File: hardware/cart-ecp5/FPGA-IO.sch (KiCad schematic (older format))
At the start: 9 parts, among them U1 LFE5U-25F-xBG256x, U5 W25Q128JVSIM

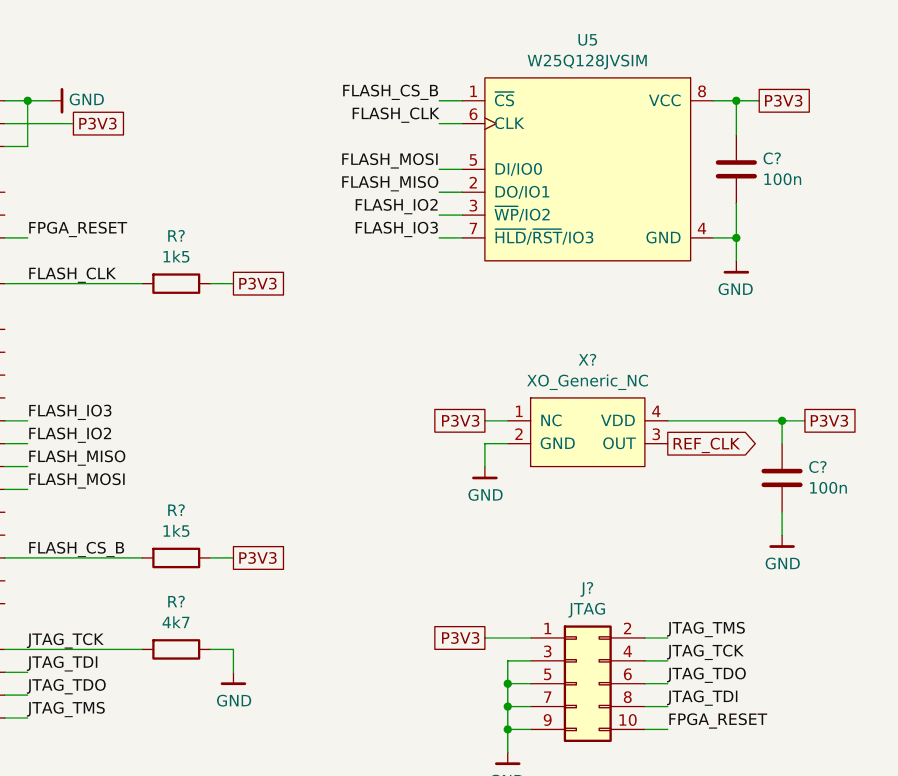
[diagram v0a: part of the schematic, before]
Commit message: First pass annotation and footprint assignment complete
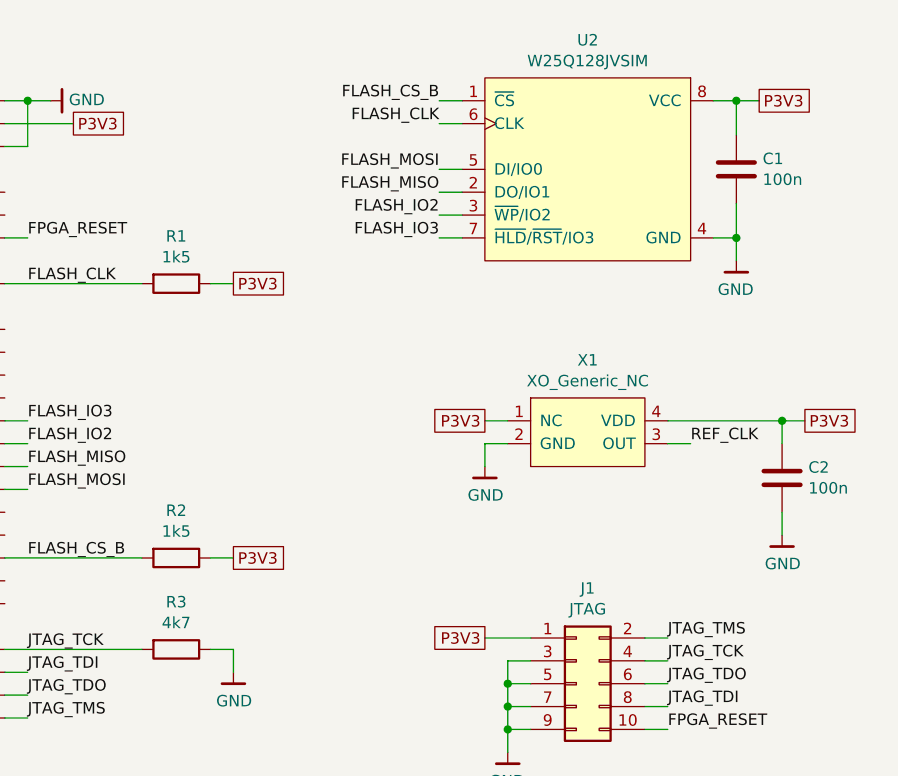
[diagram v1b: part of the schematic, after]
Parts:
- J1: renamed from J?; footprint Connector_PinHeader_1.27mm:PinHeader_2x05_P1.27mm_Vertical_SMD -> Connector_PinHeader_2.54mm:PinHeader_2x05_P2.54mm_Vertical
- R1, R2, R3: renamed from R?; footprint (none) -> Resistor_SMD:R_0603_1608Metric
- gave numbers to parts that had none: 3
- renumbered U5 to U2
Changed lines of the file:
@@
 $EndDescr
 $Comp
-L ng_memory:W25Q128JVSIM U5
+L ng_memory:W25Q128JVSIM U2
 U 1 1 5F3FC315
 P 13200 1500
-F 0 "U5" H 13650 1665 50  0000 C CNN
+F 0 "U2" H 13650 1665 50  0000 C CNN
 F 1 "W25Q128JVSIM" H 13650 1574 50  0000 C CNN
 F 2 "Package_SO:SOIC-8_5.275x5.275mm_P1.27mm" H 13700 650 50  0001 C CNN
@@
 	10200 4300 10300 4300
 $Comp
-L ng_power:GND #PWR?
+L ng_power:GND #PWR03
 U 1 1 5F643215
 P 10400 1600
-F 0 "#PWR?" H 10400 1350 50  0001 C CNN
+F 0 "#PWR03" H 10400 1350 50  0001 C CNN
 F 1 "GND" V 10404 1520 50  0000 R CNN
 F 2 "" H 10300 1250 50  0001 C CNN
@@
 	10200 2200 10300 2200
 $Comp
-L Device:R R?
+L Device:R R3
 U 1 1 5F64C834
 P 10950 4000
-F 0 "R?" V 10743 4000 50  0000 C CNN
+F 0 "R3" V 10743 4000 50  0000 C CNN
 F 1 "4k7" V 10834 4000 50  0000 C CNN
-F 2 "" V 10880 4000 50  0001 C CNN
+F 2 "Resistor_SMD:R_0603_1608Metric" V 10880 4000 50  0001 C CNN
 F 3 "~" H 10950 4000 50  0001 C CNN
 	1    10950 4000
@@
 $EndComp
 $Comp
-L Connector_Generic:Conn_02x05_Odd_Even J?
+L Connector_Generic:Conn_02x05_Odd_Even J1
 U 1 1 5F651B0D
 P 12700 4150
-F 0 "J?" H 12750 4567 50  0000 C CNN
+F 0 "J1" H 12750 4567 50  0000 C CNN
 F 1 "JTAG" H 12750 4476 50  0000 C CNN
-F 2 "Connector_PinHeader_1.27mm:PinHeader_2x05_P1.27mm_Vertical_SMD" H 12700 4150 50  0001 C CNN
+F 2 "Connector_PinHeader_2.54mm:PinHeader_2x05_P2.54mm_Vertical" H 12700 4150 50  0001 C CNN
 F 3 "~" H 12700 4150 50  0001 C CNN
 	1    12700 4150
@@
 	11200 4000 11200 4100
 $Comp
-L ng_power:GND #PWR?
+L ng_power:GND #PWR04
 U 1 1 5F666BF6
 P 11200 4100
-F 0 "#PWR?" H 11200 3850 50  0001 C CNN
+F 0 "#PWR04" H 11200 3850 50  0001 C CNN
 F 1 "GND" H 11203 3974 50  0000 C CNN
 F 2 "" H 11100 3750 50  0001 C CNN
@@
 FPGA_RESET
 $Comp
-L ng_power:GND #PWR?
+L ng_power:GND #PWR06
 U 1 1 5F676420
 P 12400 4450
-F 0 "#PWR?" H 12400 4200 50  0001 C CNN
+F 0 "#PWR06" H 12400 4200 50  0001 C CNN
 F 1 "GND" H 12403 4324 50  0000 C CNN
 F 2 "" H 12300 4100 50  0001 C CNN
@@
 $EndComp
 $Comp
-L Device:R R?
+L Device:R R1
 U 1 1 5F67946D
 P 10950 2400
-F 0 "R?" V 10743 2400 50  0000 C CNN
+F 0 "R1" V 10743 2400 50  0000 C CNN
 F 1 "1k5" V 10834 2400 50  0000 C CNN
-F 2 "" V 10880 2400 50  0001 C CNN
+F 2 "Resistor_SMD:R_0603_1608Metric" V 10880 2400 50  0001 C CNN
 F 3 "~" H 10950 2400 50  0001 C CNN
 	1    10950 2400
@@
 	11100 2400 11200 2400
 $Comp
-L Device:R R?
+L Device:R R2
 U 1 1 5F67D9E4
 P 10950 3600
-F 0 "R?" V 10743 3600 50  0000 C CNN
+F 0 "R2" V 10743 3600 50  0000 C CNN
 F 1 "1k5" V 10834 3600 50  0000 C CNN
-F 2 "" V 10880 3600 50  0001 C CNN
+F 2 "Resistor_SMD:R_0603_1608Metric" V 10880 3600 50  0001 C CNN
 F 3 "~" H 10950 3600 50  0001 C CNN
 	1    10950 3600
@@
 $EndComp
 $Comp
-L ng_time:XO_Generic_NC X?
+L ng_time:XO_Generic_NC X1
 U 1 1 5F7FED75
 P 12750 3050
-F 0 "X?" H 12750 3365 50  0000 C CNN
+F 0 "X1" H 12750 3365 50  0000 C CNN
 F 1 "XO_Generic_NC" H 12750 3274 50  0000 C CNN
 F 2 "ng_time:Oscillator_2.5x2.0" H 12750 2950 50  0001 C CNN
@@
 P3V3
 $Comp
-L ng_power:GND #PWR?
+L ng_power:GND #PWR05
 U 1 1 5F809997
 P 12300 3200
-F 0 "#PWR?" H 12300 2950 50  0001 C CNN
+F 0 "#PWR05" H 12300 2950 50  0001 C CNN
 F 1 "GND" H 12303 3074 50  0000 C CNN
 F 2 "" H 12200 2850 50  0001 C CNN
@@
 	1    0    0    -1
 $EndComp
-Text GLabel 13100 3100 2    50   Output ~ 0
-REF_CLK
-$Comp
-L Device:C C?
+$Comp
+L Device:C C1
 U 1 1 5F81782E
 P 13400 1900
-F 0 "C?" H 13515 1946 50  0000 L CNN
+F 0 "C1" H 13515 1946 50  0000 L CNN
 F 1 "100n" H 13515 1855 50  0000 L CNN
 F 2 "" H 13438 1750 50  0001 C CNN
@@
 Connection ~ 13400 2200
 $Comp
-L ng_power:GND #PWR?
+L ng_power:GND #PWR07
 U 1 1 5F8236E3
 P 13400 2300
-F 0 "#PWR?" H 13400 2050 50  0001 C CNN
+F 0 "#PWR07" H 13400 2050 50  0001 C CNN
 F 1 "GND" H 13403 2174 50  0000 C CNN
 F 2 "" H 13300 1950 50  0001 C CNN
@@
 P3V3
 $Comp
-L Device:C C?
+L Device:C C2
 U 1 1 5F839810
 P 13600 3250
-F 0 "C?" H 13715 3296 50  0000 L CNN
+F 0 "C2" H 13715 3296 50  0000 L CNN
 F 1 "100n" H 13715 3205 50  0000 L CNN
 F 2 "" H 13638 3100 50  0001 C CNN
@@
 	13600 3000 13700 3000
 $Comp
-L ng_power:GND #PWR?
+L ng_power:GND #PWR08
 U 1 1 5F83DBF8
 P 13600 3500
-F 0 "#PWR?" H 13600 3250 50  0001 C CNN
+F 0 "#PWR08" H 13600 3250 50  0001 C CNN
 F 1 "GND" H 13603 3374 50  0000 C CNN
 F 2 "" H 13500 3150 50  0001 C CNN
@@
 	13600 3000 13100 3000
 Connection ~ 13600 3000
+Wire Wire Line
+	13100 3100 13200 3100
+Text Label 13200 3100 0    50   ~ 0
+REF_CLK
 $EndSCHEMATC

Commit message: Fixes for footprint assignment
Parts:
- C1, C2: footprint (none) -> Capacitor_SMD:C_0603_1608Metric
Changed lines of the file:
@@
 F 0 "C1" H 13515 1946 50  0000 L CNN
 F 1 "100n" H 13515 1855 50  0000 L CNN
-F 2 "" H 13438 1750 50  0001 C CNN
+F 2 "Capacitor_SMD:C_0603_1608Metric" H 13438 1750 50  0001 C CNN
 F 3 "~" H 13400 1900 50  0001 C CNN
 	1    13400 1900
@@
 F 0 "C2" H 13715 3296 50  0000 L CNN
 F 1 "100n" H 13715 3205 50  0000 L CNN
-F 2 "" H 13638 3100 50  0001 C CNN
+F 2 "Capacitor_SMD:C_0603_1608Metric" H 13638 3100 50  0001 C CNN
 F 3 "~" H 13600 3250 50  0001 C CNN
 	1    13600 3250

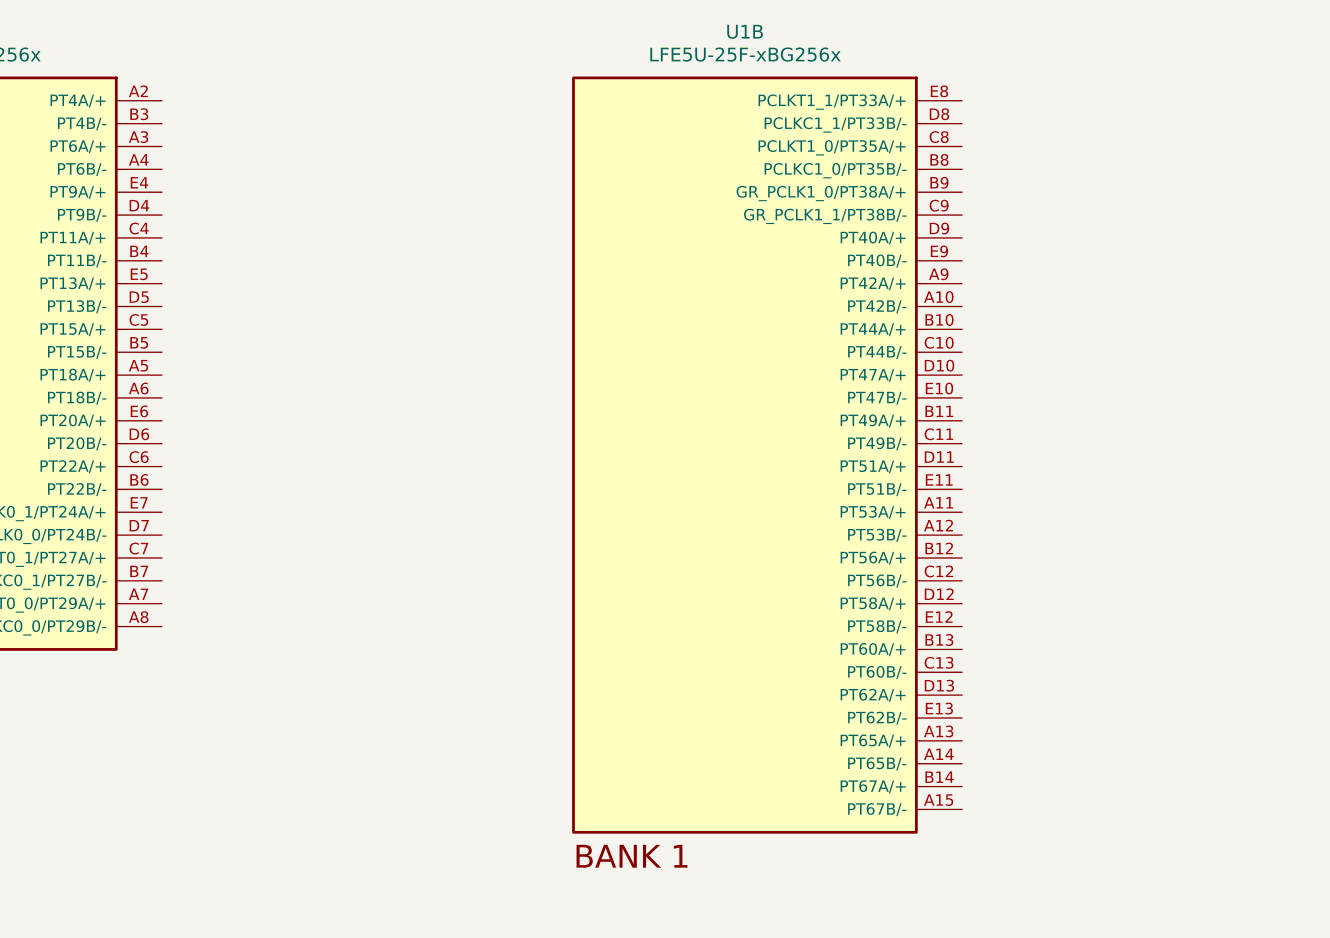
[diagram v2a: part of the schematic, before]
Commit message: Assign FPGA pins for N64 cartridge bus
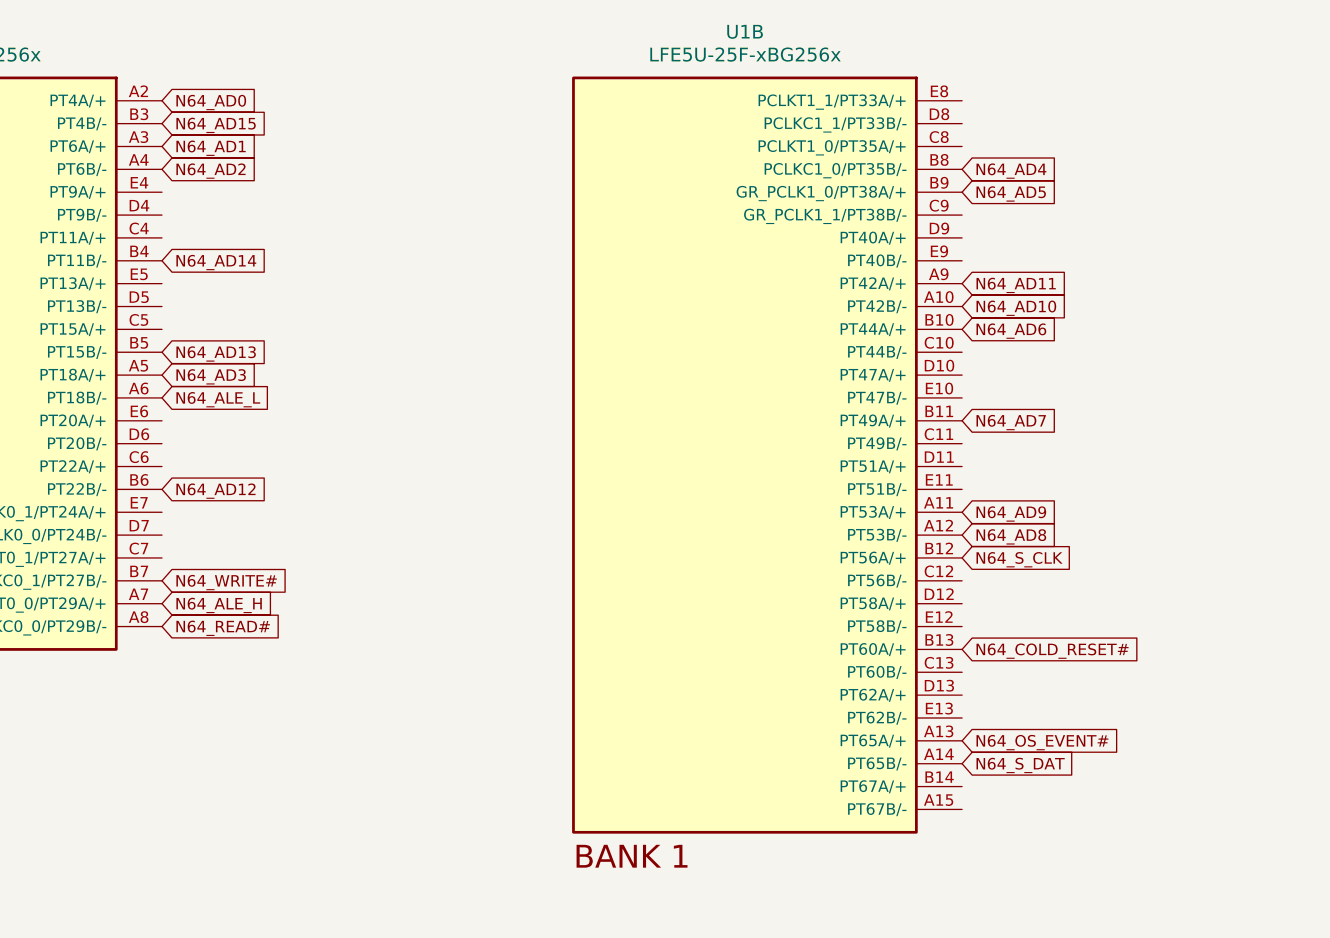
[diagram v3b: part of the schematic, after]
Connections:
- net N64_AD0: now reaches U1.A2 (PT4A/+)
- net N64_AD1: now reaches U1.A3 (PT6A/+)
- net N64_AD2: now reaches U1.A4 (PT6B/-)
- net N64_AD3: now reaches U1.A5 (PT18A/+)
- net N64_ALE_L: now reaches U1.A6 (PT18B/-)
- net N64_ALE_H: now reaches U1.A7 (PCLKT0_0/PT29A/+)
- net N64_READ#: now reaches U1.A8 (PCLKC0_0/PT29B/-)
- net N64_AD15: now reaches U1.B3 (PT4B/-)
- net N64_AD14: now reaches U1.B4 (PT11B/-)
- net N64_AD13: now reaches U1.B5 (PT15B/-)
- net N64_AD12: now reaches U1.B6 (PT22B/-)
- net N64_WRITE#: now reaches U1.B7 (PCLKC0_1/PT27B/-)
- net N64_AD10: now reaches U1.A10 (PT42B/-)
- net N64_AD9: now reaches U1.A11 (PT53A/+)
- net N64_AD8: now reaches U1.A12 (PT53B/-)
- net N64_OS_EVENT#: now reaches U1.A13 (PT65A/+)
- net N64_S_DAT: now reaches U1.A14 (PT65B/-)
- net N64_AD11: now reaches U1.A9 (PT42A/+)
- net N64_AD6: now reaches U1.B10 (PT44A/+)
- net N64_AD7: now reaches U1.B11 (PT49A/+)
- net N64_S_CLK: now reaches U1.B12 (PT56A/+)
- net N64_COLD_RESET#: now reaches U1.B13 (PT60A/+)
- net N64_AD4: now reaches U1.B8 (PCLKC1_0/PT35B/-)
- net N64_AD5: now reaches U1.B9 (GR_PCLK1_0/PT38A/+)
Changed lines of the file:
@@
 Text Label 13200 3100 0    50   ~ 0
 REF_CLK
+Text GLabel 3200 1600 2    50   Input ~ 0
+N64_AD0
+Text GLabel 3200 1700 2    50   Input ~ 0
+N64_AD15
+Text GLabel 3200 1800 2    50   Input ~ 0
+N64_AD1
+Text GLabel 3200 2300 2    50   Input ~ 0
+N64_AD14
+Text GLabel 3200 1900 2    50   Input ~ 0
+N64_AD2
+Text GLabel 3200 2700 2    50   Input ~ 0
+N64_AD13
+Text GLabel 3200 3300 2    50   Input ~ 0
+N64_AD12
+Text GLabel 6700 2400 2    50   Input ~ 0
+N64_AD11
+Text GLabel 3200 2800 2    50   Input ~ 0
+N64_AD3
+Text GLabel 6700 1900 2    50   Input ~ 0
+N64_AD4
+Text GLabel 6700 2000 2    50   Input ~ 0
+N64_AD5
+Text GLabel 6700 2500 2    50   Input ~ 0
+N64_AD10
+Text GLabel 3200 2900 2    50   Input ~ 0
+N64_ALE_L
+Text GLabel 3200 3700 2    50   Input ~ 0
+N64_WRITE#
+Text GLabel 3200 3800 2    50   Input ~ 0
+N64_ALE_H
+Text GLabel 3200 3900 2    50   Input ~ 0
+N64_READ#
+Text GLabel 6700 2600 2    50   Input ~ 0
+N64_AD6
+Text GLabel 6700 3400 2    50   Input ~ 0
+N64_AD9
+Text GLabel 6700 3000 2    50   Input ~ 0
+N64_AD7
+Text GLabel 6700 3500 2    50   Input ~ 0
+N64_AD8
+Text GLabel 6700 3600 2    50   Input ~ 0
+N64_S_CLK
+Text GLabel 6700 4400 2    50   Input ~ 0
+N64_OS_EVENT#
+Text GLabel 6700 4000 2    50   Input ~ 0
+N64_COLD_RESET#
+Text GLabel 6700 4500 2    50   Input ~ 0
+N64_S_DAT
 $EndSCHEMATC

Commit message: Shrink smallest passive to 0402
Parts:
- C1, C2: footprint Capacitor_SMD:C_0603_1608Metric -> Capacitor_SMD:C_0402_1005Metric
- R1, R2, R3: footprint Resistor_SMD:R_0603_1608Metric -> Resistor_SMD:R_0402_1005Metric
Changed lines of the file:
@@
 F 0 "R3" V 10743 4000 50  0000 C CNN
 F 1 "4k7" V 10834 4000 50  0000 C CNN
-F 2 "Resistor_SMD:R_0603_1608Metric" V 10880 4000 50  0001 C CNN
+F 2 "Resistor_SMD:R_0402_1005Metric" V 10880 4000 50  0001 C CNN
 F 3 "~" H 10950 4000 50  0001 C CNN
 	1    10950 4000
@@
 F 0 "R1" V 10743 2400 50  0000 C CNN
 F 1 "1k5" V 10834 2400 50  0000 C CNN
-F 2 "Resistor_SMD:R_0603_1608Metric" V 10880 2400 50  0001 C CNN
+F 2 "Resistor_SMD:R_0402_1005Metric" V 10880 2400 50  0001 C CNN
 F 3 "~" H 10950 2400 50  0001 C CNN
 	1    10950 2400
@@
 F 0 "R2" V 10743 3600 50  0000 C CNN
 F 1 "1k5" V 10834 3600 50  0000 C CNN
-F 2 "Resistor_SMD:R_0603_1608Metric" V 10880 3600 50  0001 C CNN
+F 2 "Resistor_SMD:R_0402_1005Metric" V 10880 3600 50  0001 C CNN
 F 3 "~" H 10950 3600 50  0001 C CNN
 	1    10950 3600
@@
 F 0 "C1" H 13515 1946 50  0000 L CNN
 F 1 "100n" H 13515 1855 50  0000 L CNN
-F 2 "Capacitor_SMD:C_0603_1608Metric" H 13438 1750 50  0001 C CNN
+F 2 "Capacitor_SMD:C_0402_1005Metric" H 13438 1750 50  0001 C CNN
 F 3 "~" H 13400 1900 50  0001 C CNN
 	1    13400 1900
@@
 F 0 "C2" H 13715 3296 50  0000 L CNN
 F 1 "100n" H 13715 3205 50  0000 L CNN
-F 2 "Capacitor_SMD:C_0603_1608Metric" H 13638 3100 50  0001 C CNN
+F 2 "Capacitor_SMD:C_0402_1005Metric" H 13638 3100 50  0001 C CNN
 F 3 "~" H 13600 3250 50  0001 C CNN
 	1    13600 3250

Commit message: Use Samtec FTSH-105 connector for JTAG
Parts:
- J1: footprint Connector_PinHeader_2.54mm:PinHeader_2x05_P2.54mm_Vertical -> ng_conn:Samtec_FTSH-105-XX-X-DV-Mating
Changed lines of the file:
@@
 F 0 "J1" H 12750 4567 50  0000 C CNN
 F 1 "JTAG" H 12750 4476 50  0000 C CNN
-F 2 "Connector_PinHeader_2.54mm:PinHeader_2x05_P2.54mm_Vertical" H 12700 4150 50  0001 C CNN
+F 2 "ng_conn:Samtec_FTSH-105-XX-X-DV-Mating" H 12700 4150 50  0001 C CNN
 F 3 "~" H 12700 4150 50  0001 C CNN
 	1    12700 4150

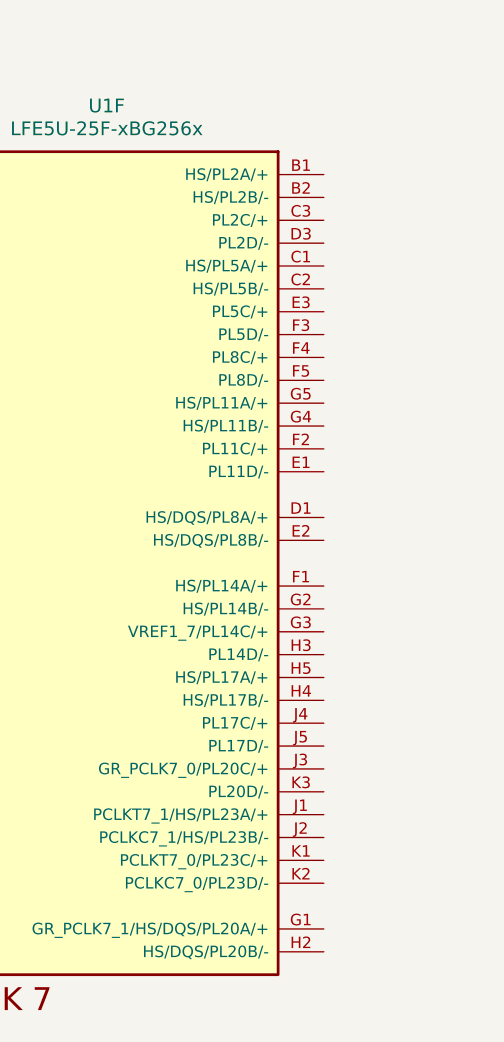
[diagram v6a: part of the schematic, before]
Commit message: Preliminary pin assignment for hyperram
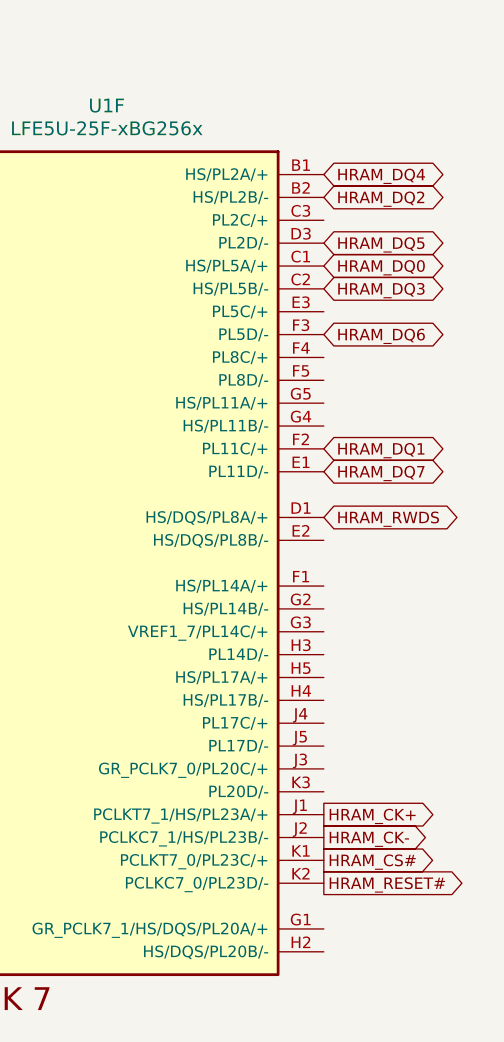
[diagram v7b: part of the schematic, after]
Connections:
- net HRAM_DQ4: now reaches U1.B1 (HS/PL2A/+)
- net HRAM_DQ2: now reaches U1.B2 (HS/PL2B/-)
- net HRAM_DQ0: now reaches U1.C1 (HS/PL5A/+)
- net HRAM_DQ3: now reaches U1.C2 (HS/PL5B/-)
- net HRAM_RWDS: now reaches U1.D1 (HS/DQS/PL8A/+)
- net HRAM_DQ5: now reaches U1.D3 (PL2D/-)
- net HRAM_DQ7: now reaches U1.E1 (PL11D/-)
- net HRAM_DQ1: now reaches U1.F2 (PL11C/+)
- net HRAM_DQ6: now reaches U1.F3 (PL5D/-)
- net HRAM_CK+: now reaches U1.J1 (PCLKT7_1/HS/PL23A/+)
- net HRAM_CK-: now reaches U1.J2 (PCLKC7_1/HS/PL23B/-)
- net HRAM_CS#: now reaches U1.K1 (PCLKT7_0/PL23C/+)
- net HRAM_RESET#: now reaches U1.K2 (PCLKC7_0/PL23D/-)
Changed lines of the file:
@@
 	1    0    0    -1
 $EndComp
+Text GLabel 13700 6000 2    50   BiDi ~ 0
+HRAM_DQ0
+Text GLabel 13700 6800 2    50   BiDi ~ 0
+HRAM_DQ1
+Text GLabel 13700 5700 2    50   BiDi ~ 0
+HRAM_DQ2
+Text GLabel 13700 6100 2    50   BiDi ~ 0
+HRAM_DQ3
+Text GLabel 13700 5600 2    50   BiDi ~ 0
+HRAM_DQ4
+Text GLabel 13700 5900 2    50   BiDi ~ 0
+HRAM_DQ5
+Text GLabel 13700 6300 2    50   BiDi ~ 0
+HRAM_DQ6
+Text GLabel 13700 6900 2    50   BiDi ~ 0
+HRAM_DQ7
+Text GLabel 13700 7100 2    50   BiDi ~ 0
+HRAM_RWDS
+Text GLabel 13700 8600 2    50   Output ~ 0
+HRAM_CS#
+Text GLabel 13700 8400 2    50   Output ~ 0
+HRAM_CK+
+Text GLabel 13700 8500 2    50   Output ~ 0
+HRAM_CK-
+Text GLabel 13700 8700 2    50   Output ~ 0
+HRAM_RESET#
 $EndSCHEMATC
